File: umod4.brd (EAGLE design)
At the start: 104.9 x 69.8 mm, 101 parts, among them IC1 27C256-FEED-THRU, M1 Generic single-sided NEO-8, M2 RPi Pico W, Q1 DNP/SI2301CDS, Q2 SS8050, U1 RP2040, U2 W25Q128JVSIQ, U3 SY6280AAC, U4 74LVC2G04, U5 74LVC541, U6 74LVC541, U7 74LVC4245, U8 TLV75733P, Y1 12MHz

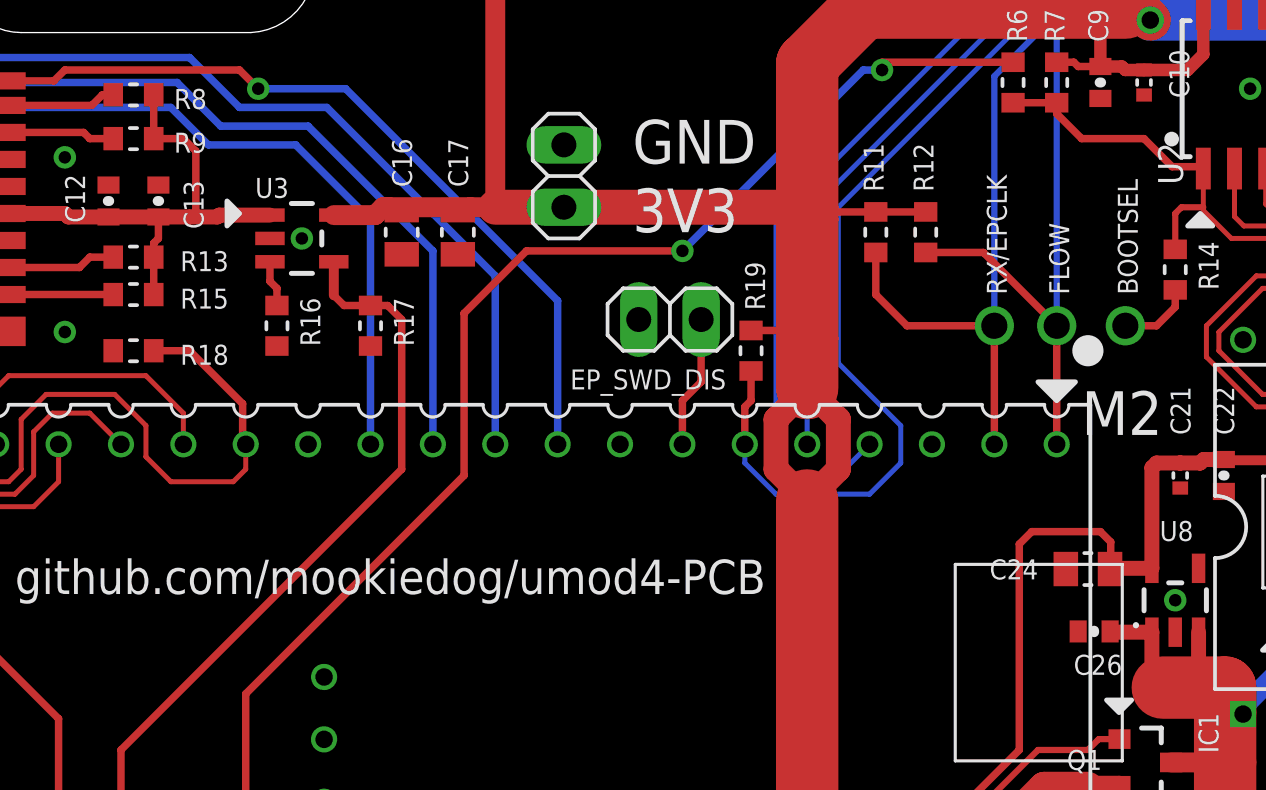
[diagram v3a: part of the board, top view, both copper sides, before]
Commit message: Replace 4u7 0402 packages with SMD-0402-NOM
- Affected parts: C13, C26
- LCSC_PART unchanged
- Manually reworked wire angles on board to clear DRC failures from the new pad geometry
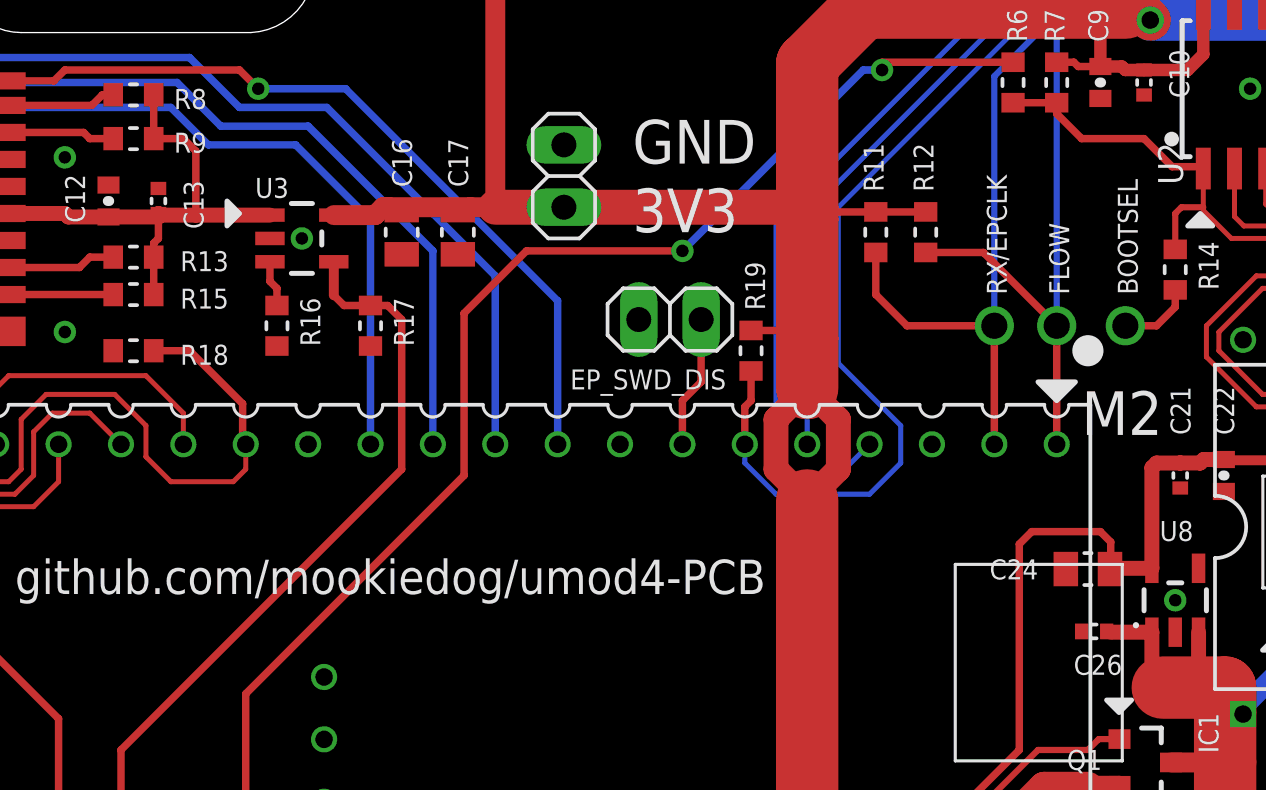
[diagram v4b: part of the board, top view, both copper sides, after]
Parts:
- C13, C26: device SparkFun-03-01-2010:0402-CAP -> robins-v7:SMD-0402-NOM
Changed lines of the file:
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@@
 <attribute name="VALUE" x="24.003" y="34.7345" size="0.4064" layer="27" rot="R90"/>
 </element>
-<element name="C13" library="SparkFun-03-01-2010" package="0402-CAP" value="4u7/10V/X5R" x="24.892" y="35.814" smashed="yes" rot="R90">
+<element name="C13" library="robins-v7" package="SMD-0402-NOM" value="4u7/10V/X5R" x="24.892" y="35.814" smashed="yes" rot="R90">
 <attribute name="LCSC_PART" value="C23733" x="24.892" y="35.814" size="1.27" layer="27" ratio="14" rot="R90" display="off"/>
 <attribute name="NAME" x="26.7335" y="34.671" size="0.8128" layer="25" ratio="14" rot="R90"/>
@@
 <attribute name="VALUE" x="60.198" y="28.194" size="0.8128" layer="27" font="vector" ratio="16"/>
 </element>
-<element name="C26" library="SparkFun-03-01-2010" package="0402-CAP" value="4u7/10V/X5R" x="62.992" y="18.288" smashed="yes" rot="R180">
+<element name="C26" library="robins-v7" package="SMD-0402-NOM" value="4u7/10V/X5R" x="62.992" y="18.288" smashed="yes" rot="R180">
 <attribute name="LCSC_PART" value="C23733" x="62.992" y="18.288" size="0.8128" layer="27" ratio="14" rot="R180" display="off"/>
 <attribute name="NAME" x="64.135" y="17.3355" size="0.8128" layer="25" font="vector" ratio="14" rot="R180"/>
@@
 </polygon>
 <contactref element="C26" pad="1"/>
-<wire x1="63.642" y1="18.288" x2="63.6721" y2="18.2579" width="0.508" layer="1"/>
 <wire x1="69.0562" y1="14.9225" x2="68.3895" y2="14.9225" width="0.2032" layer="1"/>
 <wire x1="68.3895" y1="14.9225" x2="68.326" y2="14.986" width="0.2032" layer="1"/>
@@
 <wire x1="93.106" y1="19.05" x2="93.106" y2="19.7" width="0.3048" layer="1"/>
 <wire x1="93.106" y1="19.7" x2="93.281" y2="19.875" width="0.3048" layer="1"/>
+<wire x1="63.502" y1="18.288" x2="63.6721" y2="18.288" width="0.3048" layer="1"/>
+<wire x1="63.6721" y1="18.288" x2="63.6721" y2="18.2579" width="0.3048" layer="1"/>
 </signal>
 <signal name="!RESET!_HC11_OUT">
@@
 <contactref element="R8" pad="2"/>
 <contactref element="R15" pad="2"/>
-<wire x1="22.86" y1="35.164" x2="24.892" y2="35.164" width="0.6096" layer="1"/>
-<wire x1="24.892" y1="35.164" x2="26.162" y2="35.164" width="0.6096" layer="1"/>
-<wire x1="26.162" y1="35.164" x2="27.29" y2="35.164" width="0.6096" layer="1"/>
 <wire x1="18.888" y1="35.306" x2="21.082" y2="35.306" width="0.6096" layer="1"/>
 <wire x1="22.86" y1="35.164" x2="21.224" y2="35.164" width="0.6096" layer="1"/>
 <wire x1="21.224" y1="35.164" x2="21.082" y2="35.306" width="0.6096" layer="1"/>
-<wire x1="24.892" y1="35.164" x2="24.892" y2="34.29" width="0.3048" layer="1"/>
+<wire x1="24.892" y1="35.304" x2="24.892" y2="34.29" width="0.3048" layer="1"/>
 <contactref element="R9" pad="2"/>
 <contactref element="R13" pad="2"/>
@@
 <wire x1="24.701" y1="38.354" x2="25.908" y2="38.354" width="0.3048" layer="1"/>
 <wire x1="25.908" y1="38.354" x2="26.416" y2="37.846" width="0.3048" layer="1"/>
-<wire x1="26.416" y1="37.846" x2="26.416" y2="35.418" width="0.3048" layer="1"/>
-<wire x1="26.416" y1="35.418" x2="26.162" y2="35.164" width="0.3048" layer="1"/>
 <contactref element="U3" pad="1"/>
-<wire x1="29.4339" y1="35.24" x2="27.366" y2="35.24" width="0.6096" layer="1"/>
-<wire x1="27.366" y1="35.24" x2="27.29" y2="35.164" width="0.6096" layer="1"/>
 <wire x1="24.701" y1="33.528" x2="24.701" y2="34.099" width="0.3048" layer="1"/>
 <wire x1="24.701" y1="34.099" x2="24.892" y2="34.29" width="0.3048" layer="1"/>
+<wire x1="29.4339" y1="35.24" x2="26.416" y2="35.24" width="0.6096" layer="1"/>
+<wire x1="26.416" y1="35.24" x2="24.892" y2="35.24" width="0.6096" layer="1"/>
+<wire x1="24.892" y1="35.24" x2="24.892" y2="35.304" width="0.6096" layer="1"/>
+<wire x1="22.86" y1="35.164" x2="24.892" y2="35.164" width="0.6096" layer="1"/>
+<wire x1="24.892" y1="35.164" x2="24.892" y2="35.304" width="0.6096" layer="1"/>
+<wire x1="26.416" y1="37.846" x2="26.416" y2="35.24" width="0.3048" layer="1"/>
 </signal>
 <signal name="EP_BOOTSEL">

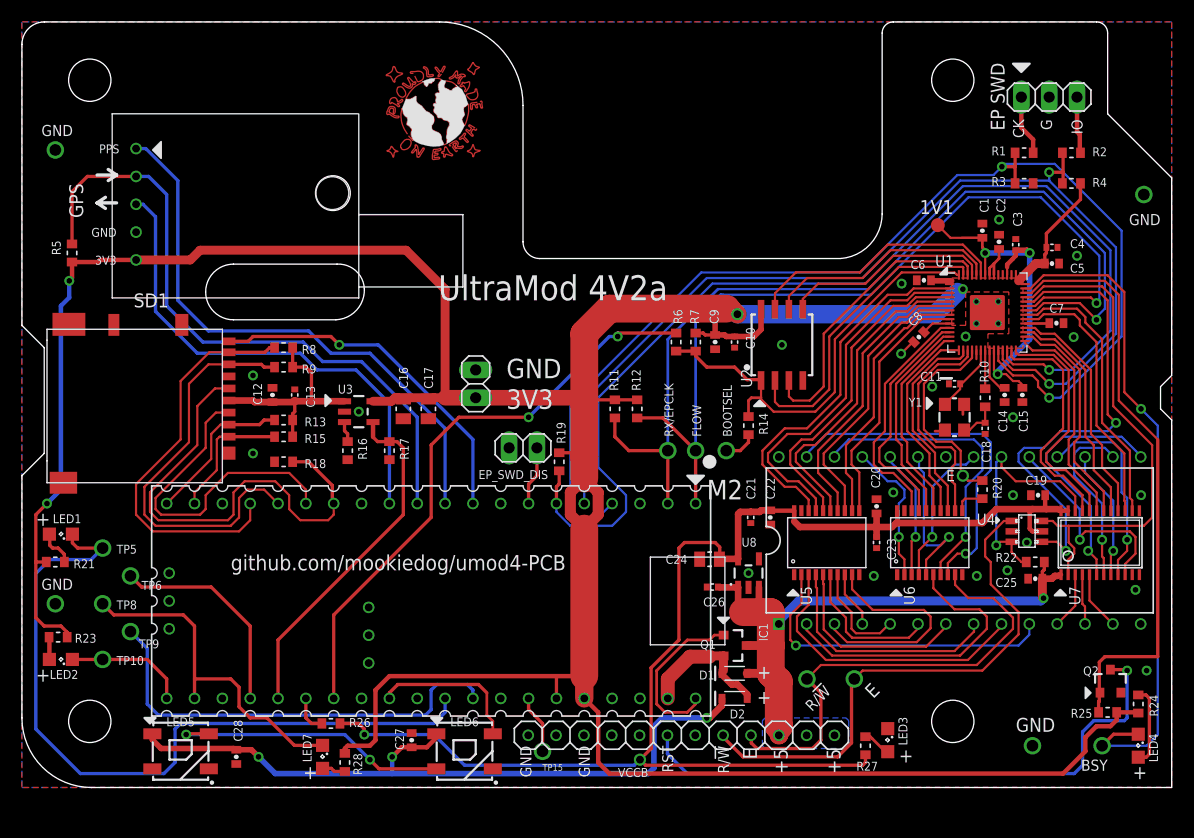
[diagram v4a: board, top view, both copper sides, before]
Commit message: Replace all 100nF 0402 packages with SMD-0402-NOM
- Affected parts: C1, C2, C5, C6, C7, C8, C9, C12, C14, C15, C19, C20, C22, C25, C27, C28
- LCSC_PART unchanged
- Manually reworked wire angles on board to clear DRC failures from the new pad geometry
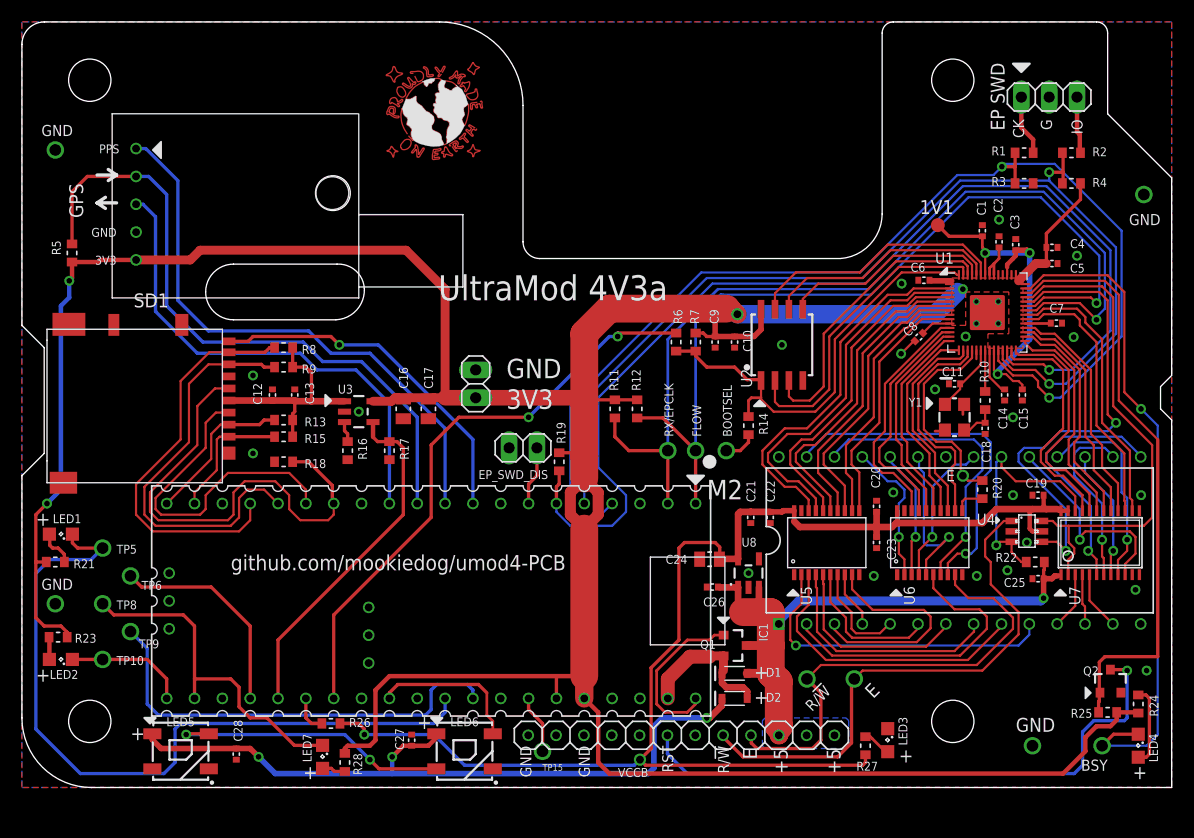
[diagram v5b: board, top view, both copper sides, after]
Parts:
- C1, C12, C14, C15, C19, C2, C20, C22, C25, C27, C28, C5, C6, C7, C8, C9: device SparkFun-03-01-2010:0402-CAP -> robins-v7:SMD-0402-NOM
- moved R10 0.25 mm to (87.9, 35.3)
- moved C28 0.25 mm to (19.6, 3.05)
- moved C25 0.25 mm to (92.7, 19.1)
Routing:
- net 1.0V: track 35.4 -> 33.8 mm
- net +3V3: track 317.7 -> 318.6 mm
- net VSYS: track 13.2 -> 13.8 mm
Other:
- board text added: "UltraMod 4V3a"
- board text removed: "UltraMod 4V2a"

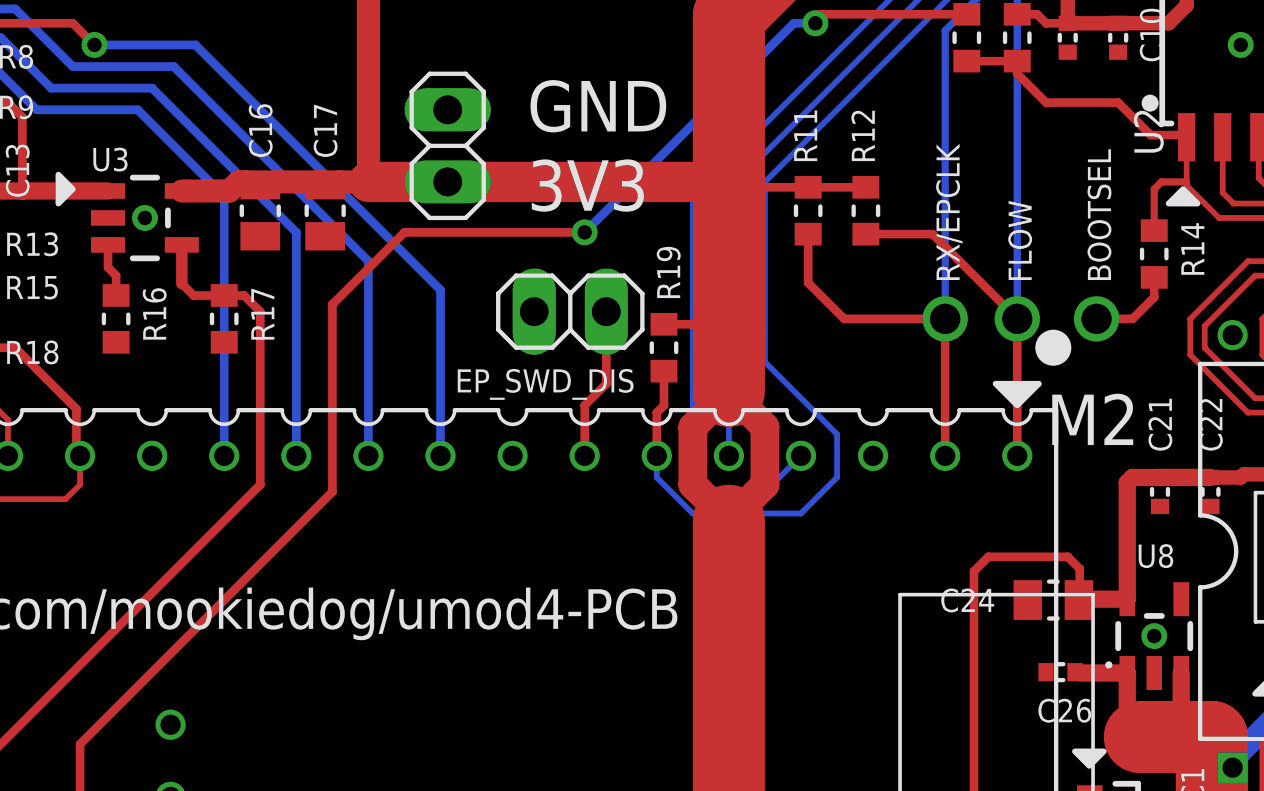
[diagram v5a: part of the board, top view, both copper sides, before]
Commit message: Replace all 10uF 0805 packages with SMD-0805-NOM
- Affected parts: C16, C17, C24
- LCSC_PART unchanged
- Manually reworked wire angles on board to clear DRC failures from the new pad geometry
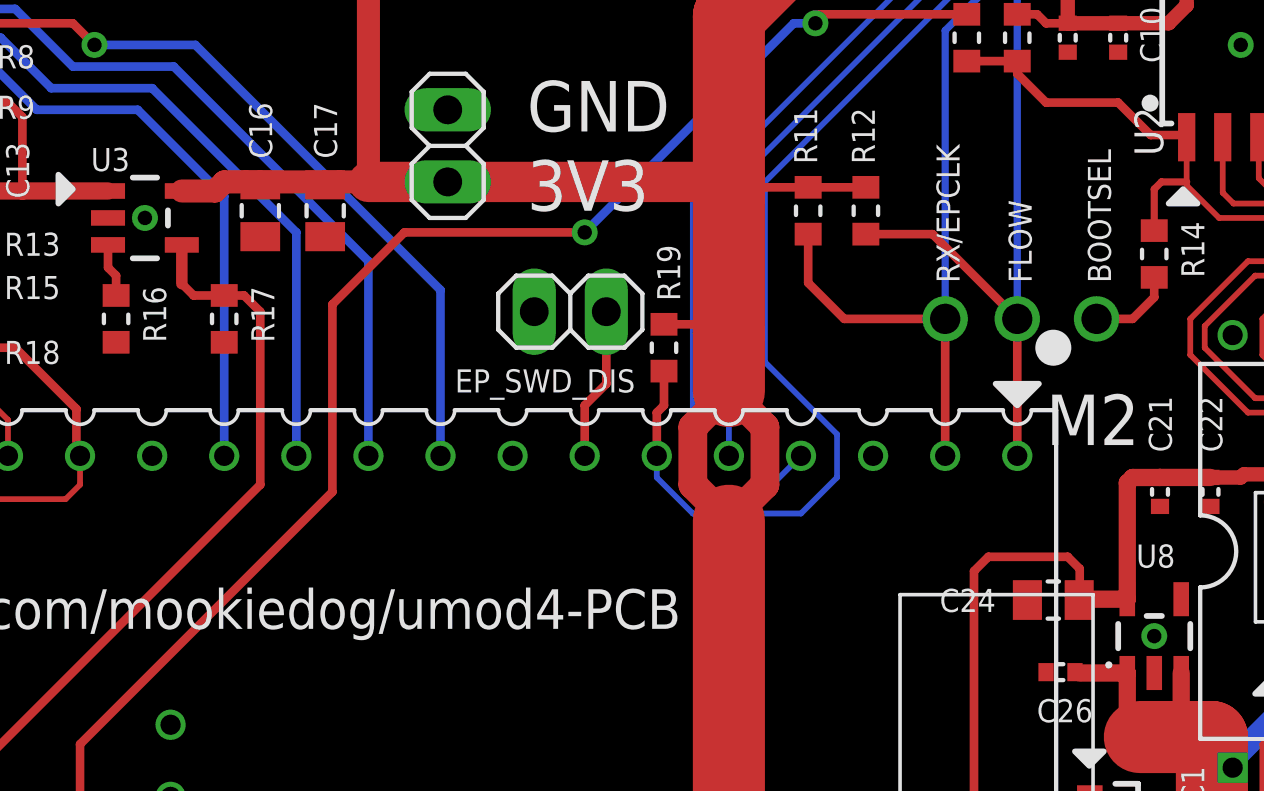
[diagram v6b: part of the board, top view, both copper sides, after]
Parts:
- C16, C17, C24: device robins-v7:SMD-0805 -> robins-v7:SMD-0805-NOM
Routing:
- net +3V3: track 318.6 -> 317.8 mm
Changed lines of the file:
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@@
 <attribute name="VALUE" x="46.228" y="0.762" size="0.8128" layer="27" font="vector" ratio="16"/>
 </element>
-<element name="C24" library="robins-v7" package="SMD-0805" value="10u/25V/X5R" x="62.738" y="20.828" smashed="yes" rot="R180">
+<element name="C24" library="robins-v7" package="SMD-0805-NOM" value="10u/25V/X5R" x="62.738" y="20.828" smashed="yes" rot="R180">
 <attribute name="LCSC_PART" value="C15850" x="62.738" y="20.828" size="1.778" layer="27" rot="R180" display="off"/>
 <attribute name="NAME" x="58.734" y="20.4075" size="0.8128" layer="25" font="vector" ratio="14"/>
 <attribute name="VALUE" x="63.754" y="22.479" size="0.8128" layer="27" font="vector" ratio="16" rot="R180"/>
 </element>
-<element name="C16" library="robins-v7" package="SMD-0805" value="10u/25V/X5R" x="34.798" y="34.544" smashed="yes" rot="R270">
+<element name="C16" library="robins-v7" package="SMD-0805-NOM" value="10u/25V/X5R" x="34.798" y="34.544" smashed="yes" rot="R270">
 <attribute name="LCSC_PART" value="C15850" x="35.052" y="34.544" size="1.778" layer="27" rot="R270" display="off"/>
 <attribute name="NAME" x="35.2185" y="36.382" size="0.8128" layer="25" font="vector" ratio="14" rot="R90"/>
 <attribute name="VALUE" x="33.147" y="35.56" size="0.8128" layer="27" font="vector" ratio="16" rot="R270"/>
 </element>
-<element name="C17" library="robins-v7" package="SMD-0805" value="10u/25V/X5R" x="37.084" y="34.544" smashed="yes" rot="R270">
+<element name="C17" library="robins-v7" package="SMD-0805-NOM" value="10u/25V/X5R" x="37.084" y="34.544" smashed="yes" rot="R270">
 <attribute name="LCSC_PART" value="C15850" x="37.338" y="34.544" size="1.778" layer="27" rot="R270" display="off"/>
 <attribute name="NAME" x="37.5045" y="36.382" size="0.8128" layer="25" font="vector" ratio="14" rot="R90"/>
@@
 <wire x1="41.402" y1="35.56" x2="38.608" y2="35.56" width="1.4224" layer="1"/>
 <contactref element="U3" pad="5"/>
-<wire x1="32.0341" y1="35.24" x2="33.716" y2="35.24" width="0.8128" layer="1"/>
+<wire x1="32.0341" y1="35.24" x2="33.208" y2="35.24" width="0.8128" layer="1"/>
 <contactref element="M1" pad="5"/>
 <contactref element="R5" pad="2"/>
@@
 <wire x1="1.27" y1="24.892" x2="2.286" y2="25.908" width="0.3048" layer="1"/>
 <wire x1="2.223" y1="20.574" x2="1.27" y2="20.574" width="0.3048" layer="1"/>
-<wire x1="33.716" y1="35.24" x2="34.036" y2="35.56" width="0.8128" layer="1"/>
-<wire x1="34.036" y1="35.56" x2="34.29" y2="35.56" width="0.8128" layer="1"/>
-<wire x1="34.29" y1="35.56" x2="37.592" y2="35.56" width="0.8128" layer="1"/>
+<wire x1="33.208" y1="35.24" x2="33.528" y2="35.56" width="0.8128" layer="1"/>
+<wire x1="33.528" y1="35.56" x2="34.29" y2="35.56" width="0.8128" layer="1"/>
+<wire x1="34.29" y1="35.56" x2="34.798" y2="35.56" width="0.8128" layer="1"/>
+<wire x1="34.798" y1="35.56" x2="37.084" y2="35.56" width="0.8128" layer="1"/>
+<wire x1="37.084" y1="35.56" x2="37.592" y2="35.56" width="0.8128" layer="1"/>
 <wire x1="37.592" y1="35.56" x2="38.608" y2="35.56" width="0.8128" layer="1"/>
 <wire x1="38.608" y1="45.466" x2="38.608" y2="35.56" width="0.8128" layer="1"/>
@@
 <contactref element="C16" pad="1"/>
 <contactref element="C17" pad="1"/>
-<wire x1="34.798" y1="35.444" x2="34.29" y2="35.444" width="0.4064" layer="1"/>
 <wire x1="34.29" y1="35.444" x2="34.29" y2="35.56" width="0.4064" layer="1"/>
-<wire x1="37.084" y1="35.444" x2="37.592" y2="35.444" width="0.4064" layer="1"/>
 <wire x1="29.464" y1="3.111" x2="29.464" y2="3.556" width="0.4064" layer="1"/>
 <wire x1="29.464" y1="3.556" x2="29.718" y2="3.81" width="0.4064" layer="1"/>
@@
 <wire x1="82.30881875" y1="41.55681875" x2="82.29841875" y2="41.55681875" width="0.2032" layer="1"/>
 <wire x1="82.29841875" y1="41.55681875" x2="82.199421875" y2="41.457821875" width="0.2032" layer="1"/>
+<wire x1="34.798" y1="35.4565" x2="34.798" y2="35.56" width="0.254" layer="1"/>
+<wire x1="37.084" y1="35.4565" x2="37.084" y2="35.56" width="0.254" layer="1"/>
 </signal>
 <signal name="R/!W!_5V">
@@
 <contactref element="C24" pad="1"/>
 <wire x1="63.6681" y1="20.574" x2="63.6681" y2="20.8581" width="0.4064" layer="1"/>
-<wire x1="63.638" y1="20.828" x2="63.754" y2="20.828" width="0.4064" layer="1"/>
+<wire x1="63.6505" y1="20.828" x2="63.754" y2="20.828" width="0.4064" layer="1"/>
 <wire x1="63.754" y1="20.828" x2="63.754" y2="20.8581" width="0.4064" layer="1"/>
 <wire x1="56.896" y1="2.032" x2="56.388" y2="2.54" width="0.3048" layer="1"/>
